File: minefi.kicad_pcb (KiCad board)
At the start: 2 copper layers, 130.8 x 95.2 mm, 152 parts, among them P1 CONN_25X2, P11 CONN_1, P13 CONN_1, P16 CONN_1, P18 CONN_1, P2 CONN_25X2, P20 CONN_1, P21 CONN_1, P23 CONN_1, P4 CONN_25, P5 CONN_3X2, P51 CONN_1, P52 CONN_1, Q1001 MOS_PRO, Q401 OVP_DRIVER, Q402 OVP_DRIVER, Q403 OVP_DRIVER, Q404 OVP_DRIVER, U1001 LM2596, U101 MAX9926/9927, U201 MCP6004, U202 MCP6004

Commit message: progress
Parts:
- removed P20, P21, P23: CONN_1, SIL-1
- C1001, C1002, C1003, D1001, D1002, D1003, D1004, D1005, D1006, L1001, L1002, Q1001, R1001, R1002, R320, R321, U1001, W23: moved to F.Cu
- moved C23 85.6 mm to (14.0, 85.1)
- moved C24 85.6 mm to (14.0, 82.5)
- moved D1002 72.2 mm to (86.4, 31.8), turned to 180 degrees
- moved D1005 71.7 mm to (102.9, 24.1), turned to 270 degrees
- moved D1003 69.0 mm to (86.4, 29.2), turned to 180 degrees
- moved R1002 67.6 mm to (102.9, 20.3), turned to 270 degrees
- moved Q1001 56.7 mm to (62.2, 11.4), turned to 0 degrees
- moved D1001 54.3 mm to (58.4, 17.8), turned to 0 degrees
- moved F1001 53.0 mm to (55.9, 5.08), turned to 0 degrees
- moved R1001 52.9 mm to (57.1, 10.2)
- moved C1001 52.1 mm to (71.1, 15.2)
- moved L1001 50.6 mm to (102.9, 8.89)
- moved R210 47.7 mm to (67.3, 59.7)
- moved R213 47.7 mm to (81.3, 58.4)
- moved R214 47.7 mm to (102.9, 58.4)
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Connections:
- P2 pad 29: /inj_12ch/INJ-10_5V -> (no net)
- P2 pad 31: /inj_12ch/INJ-07_5V -> (no net)
- P4 pad 7: /cps_vrs_io_1/CAM+ -> /cps_vrs_io_1/CAM-
- P4 pad 8: /cps_vrs_io_1/CAM- -> /cps_vrs_io_1/CAM+
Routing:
- net /adc_amp_divider/5V: track 320.7 -> 413.6 mm, vias 8 -> 5
- net GND: track 783.7 -> 849.4 mm, vias 2 -> 1
- net /stm32f407_board/3.3V: track 152.8 -> 89.8 mm
- net /adc_amp_divider/OUT4: track 14.8 -> 64.6 mm
- net /adc_amp_divider/OUT2: track 22.1 -> 60.6 mm
- net /adc_amp_divider/INP5: track 108.5 -> 71.2 mm, vias 0 -> 1
- net /adc_amp_divider/INP4: track 34.5 -> 70.5 mm
- net /adc_amp_divider/INP1: track 47.1 -> 79.9 mm, vias 1 -> 0
- net /adc_amp_divider/INP2: track 45.6 -> 74.9 mm, vias 1 -> 0
- net /adc_amp_divider/OUT3: track 25.8 -> 54.1 mm
- net /adc_amp_divider/INP3: track 36.0 -> 63.5 mm
- net /stm32f407_board/PC11: track 140.8 -> 117.0 mm, vias 0 -> 1
- net /adc_amp_divider/INP12: track 153.9 -> 131.0 mm, vias 2 -> 0
- net /PWR_buck_12V_switcher/FB: track 62.5 -> 42.8 mm
- net N-00000181: track 21.4 -> 1.91 mm
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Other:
- net class power removed

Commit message: vias and fill zones
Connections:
- hole1 pad 1: (no net) -> GND
- hole2 pad 1: (no net) -> GND
- hole3 pad 1: (no net) -> GND
- hole4 pad 1: (no net) -> GND
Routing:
- net GND: track 849.4 -> 865.8 mm
- net /PWR_buck_12V_switcher/VBAT: track 42.6 -> 38.8 mm
- net /PWR_buck_12V_switcher/Vf: track 8.54 -> 7.35 mm
- net (no net): vias 0 -> 196
- added copper zone on F.Cu, net (none)
- added copper zone on B.Cu, net GND
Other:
- net class Default: clearance 0.254 -> 0.1778
- rule trace_clearance: 0.254 -> 0.1778

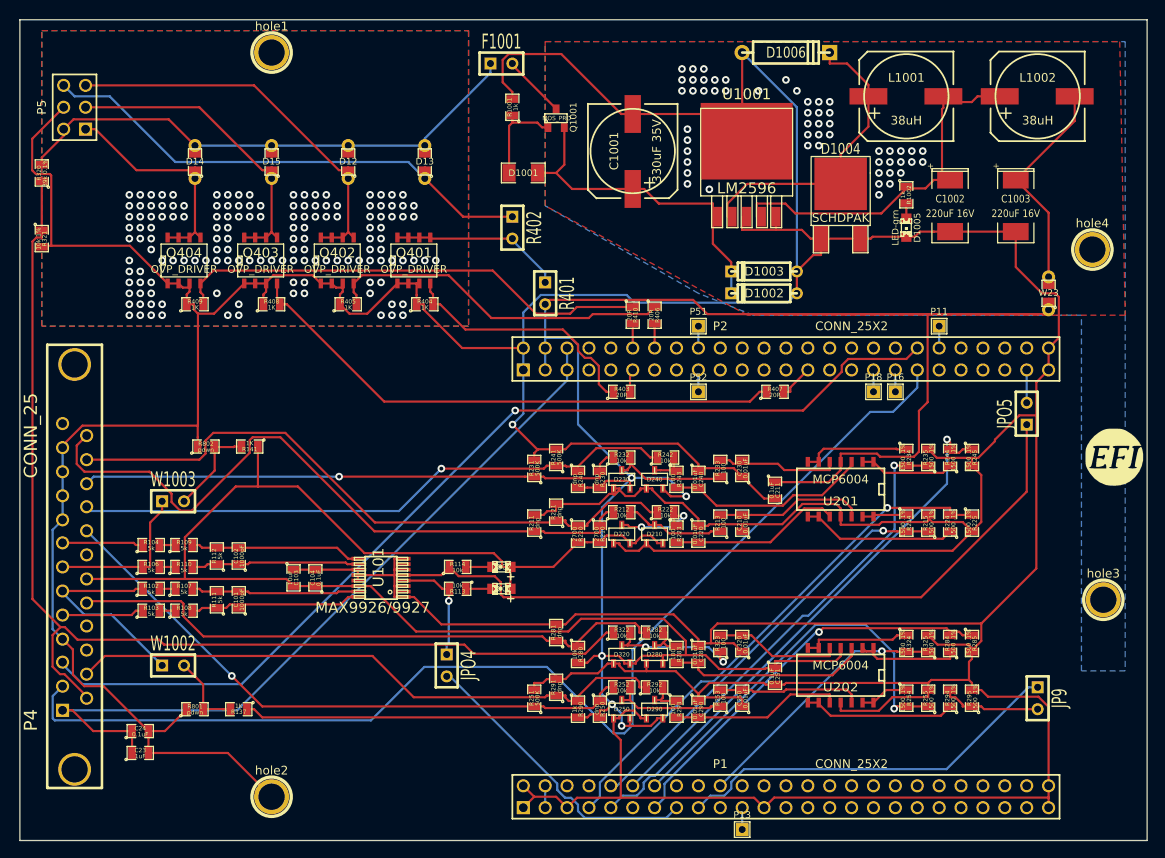
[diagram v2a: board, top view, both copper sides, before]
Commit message: more width of power lines
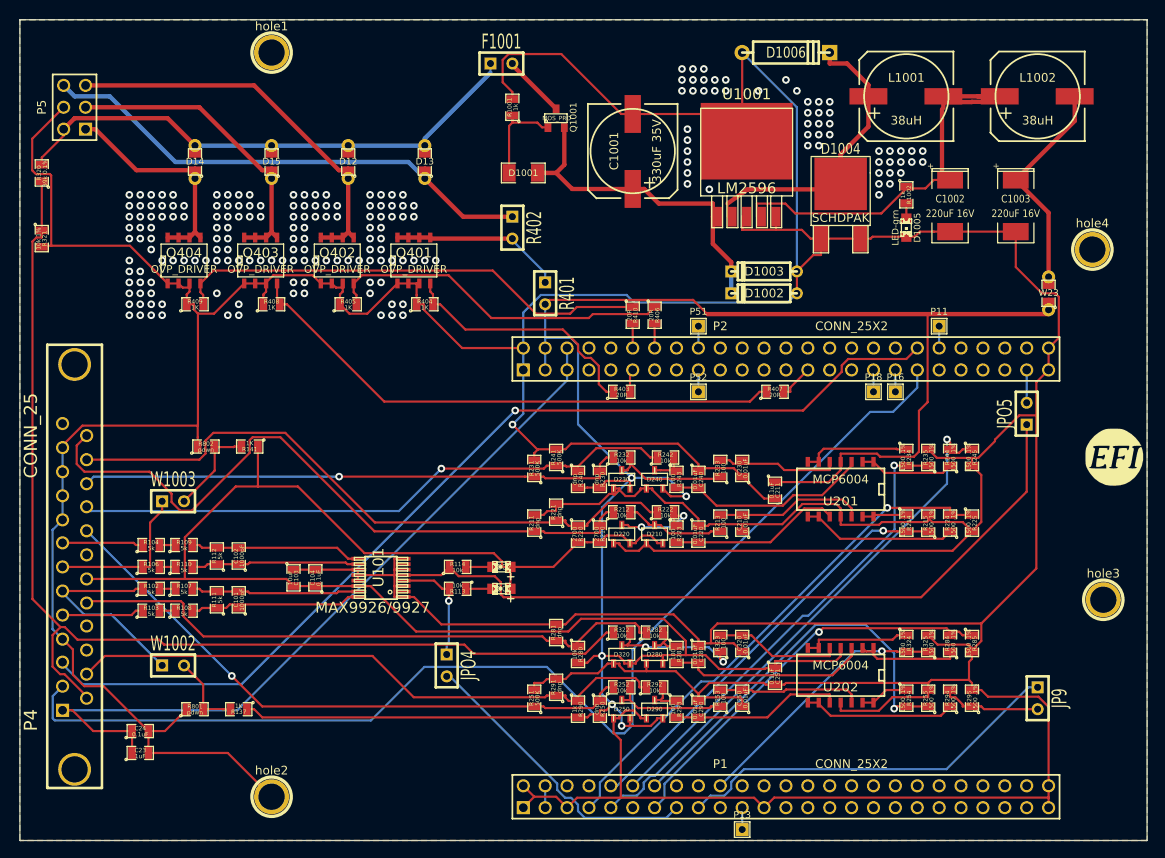
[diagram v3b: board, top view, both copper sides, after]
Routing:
- net /PWR_buck_12V_switcher/FB: track 42.8 -> 51.9 mm
- added copper zone on F.Cu, net GND
- removed copper zone on F.Cu, net (none)
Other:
- net class power added: clearance 0.1778, trace_width 0.508, via_dia 0.889, via_drill 0.635

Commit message: wider wires
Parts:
- moved P5 180.7 mm to (183.5, 45.7), turned to 0 degrees
- moved R320 175.0 mm to (175.9, 41.9), turned to 0 degrees
- moved hole1 173.2 mm to (189.9, 68.6), turned to 270 degrees
- moved R321 166.6 mm to (168.3, 41.9), turned to 180 degrees
- moved L1002 162.9 mm to (184.8, 157.5), turned to 270 degrees
- moved D14 162.7 mm to (177.2, 59.7), turned to 0 degrees
- moved F1001 160.4 mm to (188.6, 95.2), turned to 270 degrees
- moved D1006 160.3 mm to (189.9, 128.3), turned to 270 degrees
- moved D15 156.9 mm to (177.2, 68.6), turned to 0 degrees
- moved L1001 156.5 mm to (184.8, 142.2), turned to 270 degrees
- moved R1001 153.1 mm to (183.5, 96.5), turned to 0 degrees
- moved D12 151.8 mm to (177.2, 77.5), turned to 0 degrees
- moved Q1001 150.1 mm to (182.2, 101.6), turned to 270 degrees
- moved Q404 149.8 mm to (165.7, 58.4), turned to 270 degrees
- moved D13 147.7 mm to (177.2, 86.4), turned to 0 degrees
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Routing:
- net /PWR_buck_12V_switcher/FB: track 51.9 -> 49.4 mm
- net /adc_amp_divider/12V_bat: track 65.4 -> 67.6 mm
- net /inj_12ch/INJ-01_2: track 59.3 -> 57.2 mm
- net /inj_12ch/INJ-02: track 46.1 -> 47.5 mm
- net /adc_amp_divider/5V: track 413.6 -> 414.7 mm
- net /inj_12ch/INJ-01: track 20.0 -> 19.5 mm
- net (no net): vias 196 -> 190
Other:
- board size 130.8 x 95.2 mm -> 95.3 x 130.8 mm
- net class power: trace_width 0.508 -> 0.762

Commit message: progress
board is better
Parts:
- moved D14 57.2 mm to (135.1, 98.6)
- moved D12 53.6 mm to (135.1, 110.7)
- moved D15 48.1 mm to (142.2, 101.6), turned to 180 degrees
- moved D210 46.4 mm to (102.0, 146.6)
- moved D220 46.4 mm to (102.0, 142.8)
- moved D230 46.4 mm to (108.3, 142.8)
- moved D240 46.4 mm to (108.3, 146.6)
- moved D802 46.4 mm to (98.2, 128.8)
- moved R223 46.4 mm to (102.0, 149.1)
- moved R243 46.4 mm to (108.3, 149.1)
- moved R802 46.4 mm to (112.1, 94.5)
- moved C1002 46.4 mm to (140.1, 180.9)
- moved C1003 46.4 mm to (140.1, 188.5)
- moved C210 46.4 mm to (103.3, 156.7)
- moved C211 46.4 mm to (107.1, 160.6)
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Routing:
- net GND: track 865.8 -> 1084.0 mm, vias 1 -> 99
- net /inj_12ch/INJ-03_5V: track 4.21 -> 72.2 mm
- net /inj_12ch/INJ-04_5V: track 2.86 -> 59.4 mm, vias 0 -> 1
- net N-00000131: track 64.4 -> 12.5 mm
- net N-00000129: track 55.7 -> 4.78 mm
- net /inj_12ch/INJ-02_5V: track 2.86 -> 48.6 mm
- net /inj_12ch/INJ-01_5V: track 2.67 -> 38.9 mm
- net N-00000127: track 40.5 -> 4.78 mm
- net /adc_amp_divider/5V: track 414.7 -> 432.3 mm
- net N-00000132: track 29.4 -> 12.6 mm
- net /adc_amp_divider/12V_bat: track 67.6 -> 79.9 mm
- net /inj_12ch/INJ-01_2: track 57.2 -> 46.4 mm
- net /inj_12ch/INJ-01: track 19.5 -> 12.8 mm
- net /inj_12ch/INJ-04: track 26.6 -> 33.1 mm
- net /inj_12ch/INJ-03: track 36.5 -> 30.7 mm
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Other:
- net class .02 added: clearance 0.2032, trace_width 0.508, via_dia 0.889, via_drill 0.635
- net class Default: clearance 0.1778 -> 0.2032
- net class power removed
- rule pad_to_mask_clearance: 0.2 -> 0
- rule trace_clearance: 0.1778 -> 0.2032

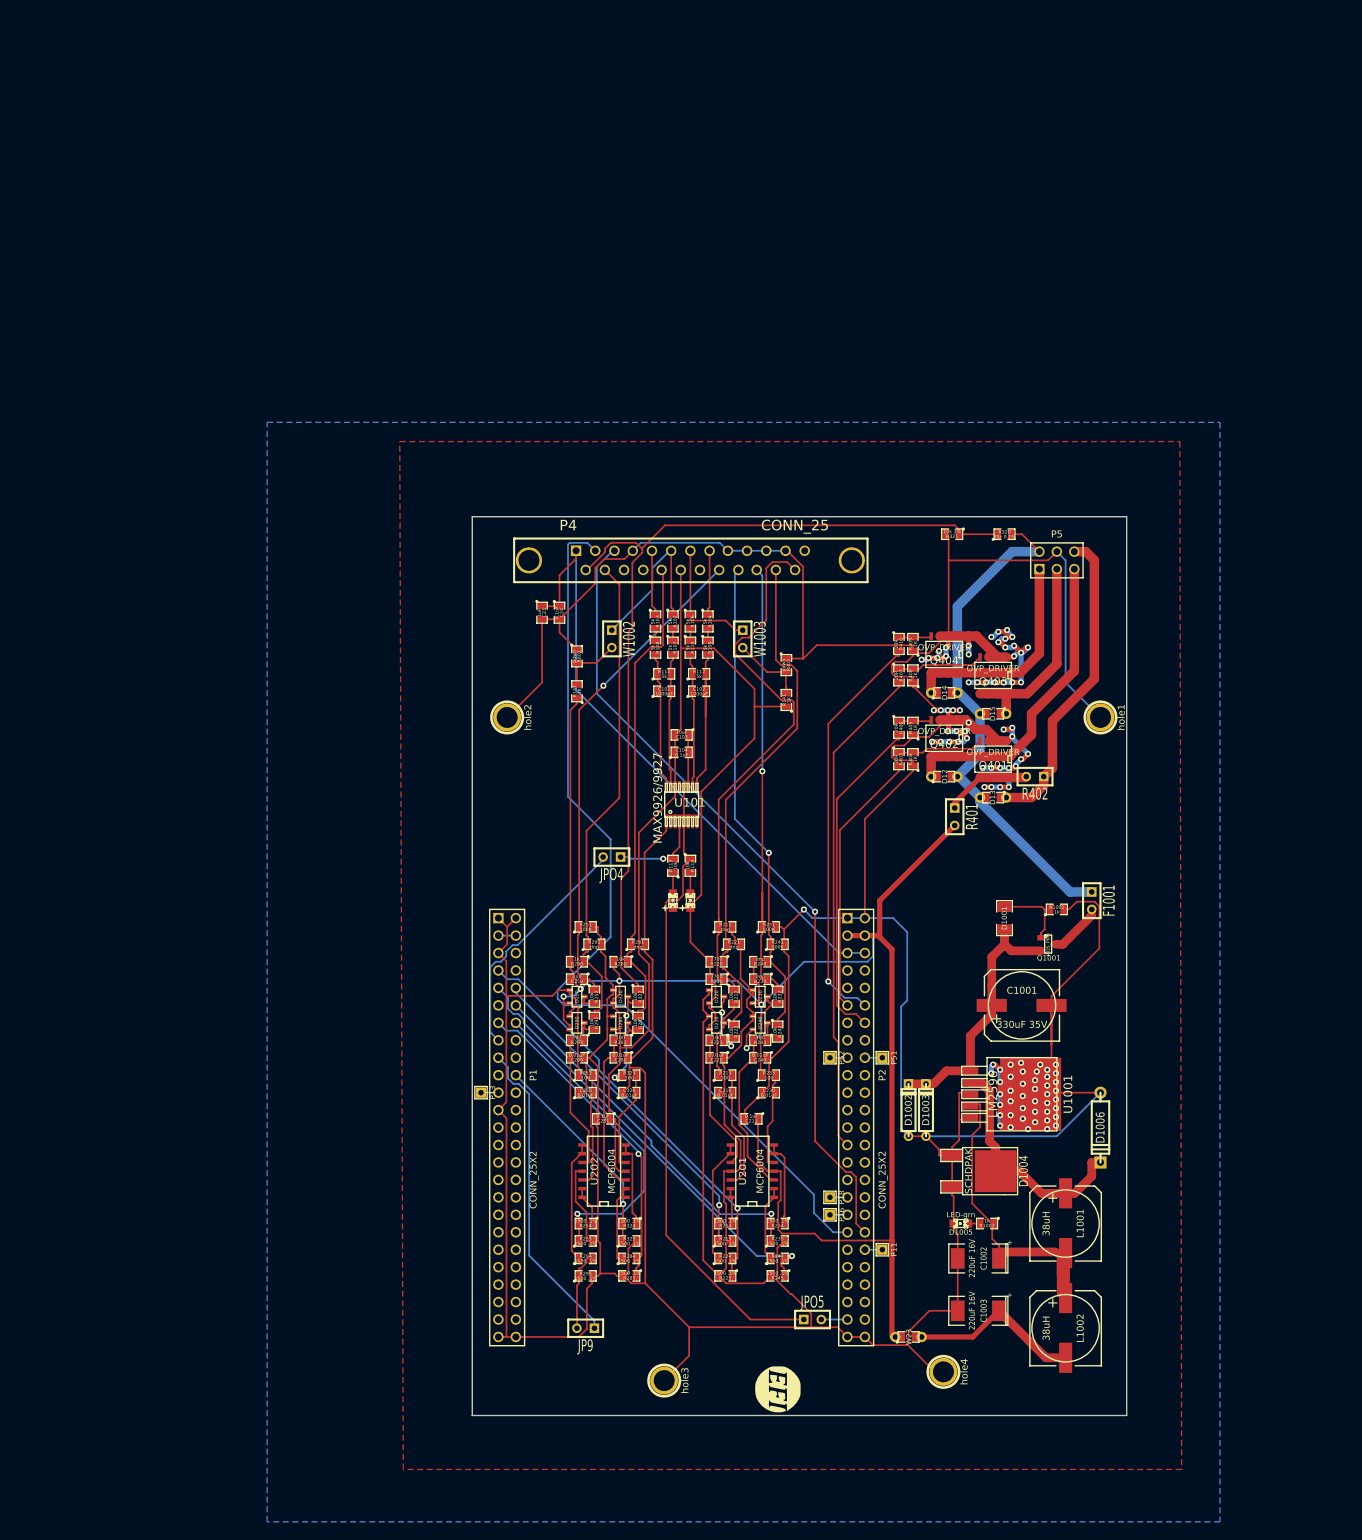
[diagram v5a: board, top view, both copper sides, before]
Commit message: vr input changed to lm1815
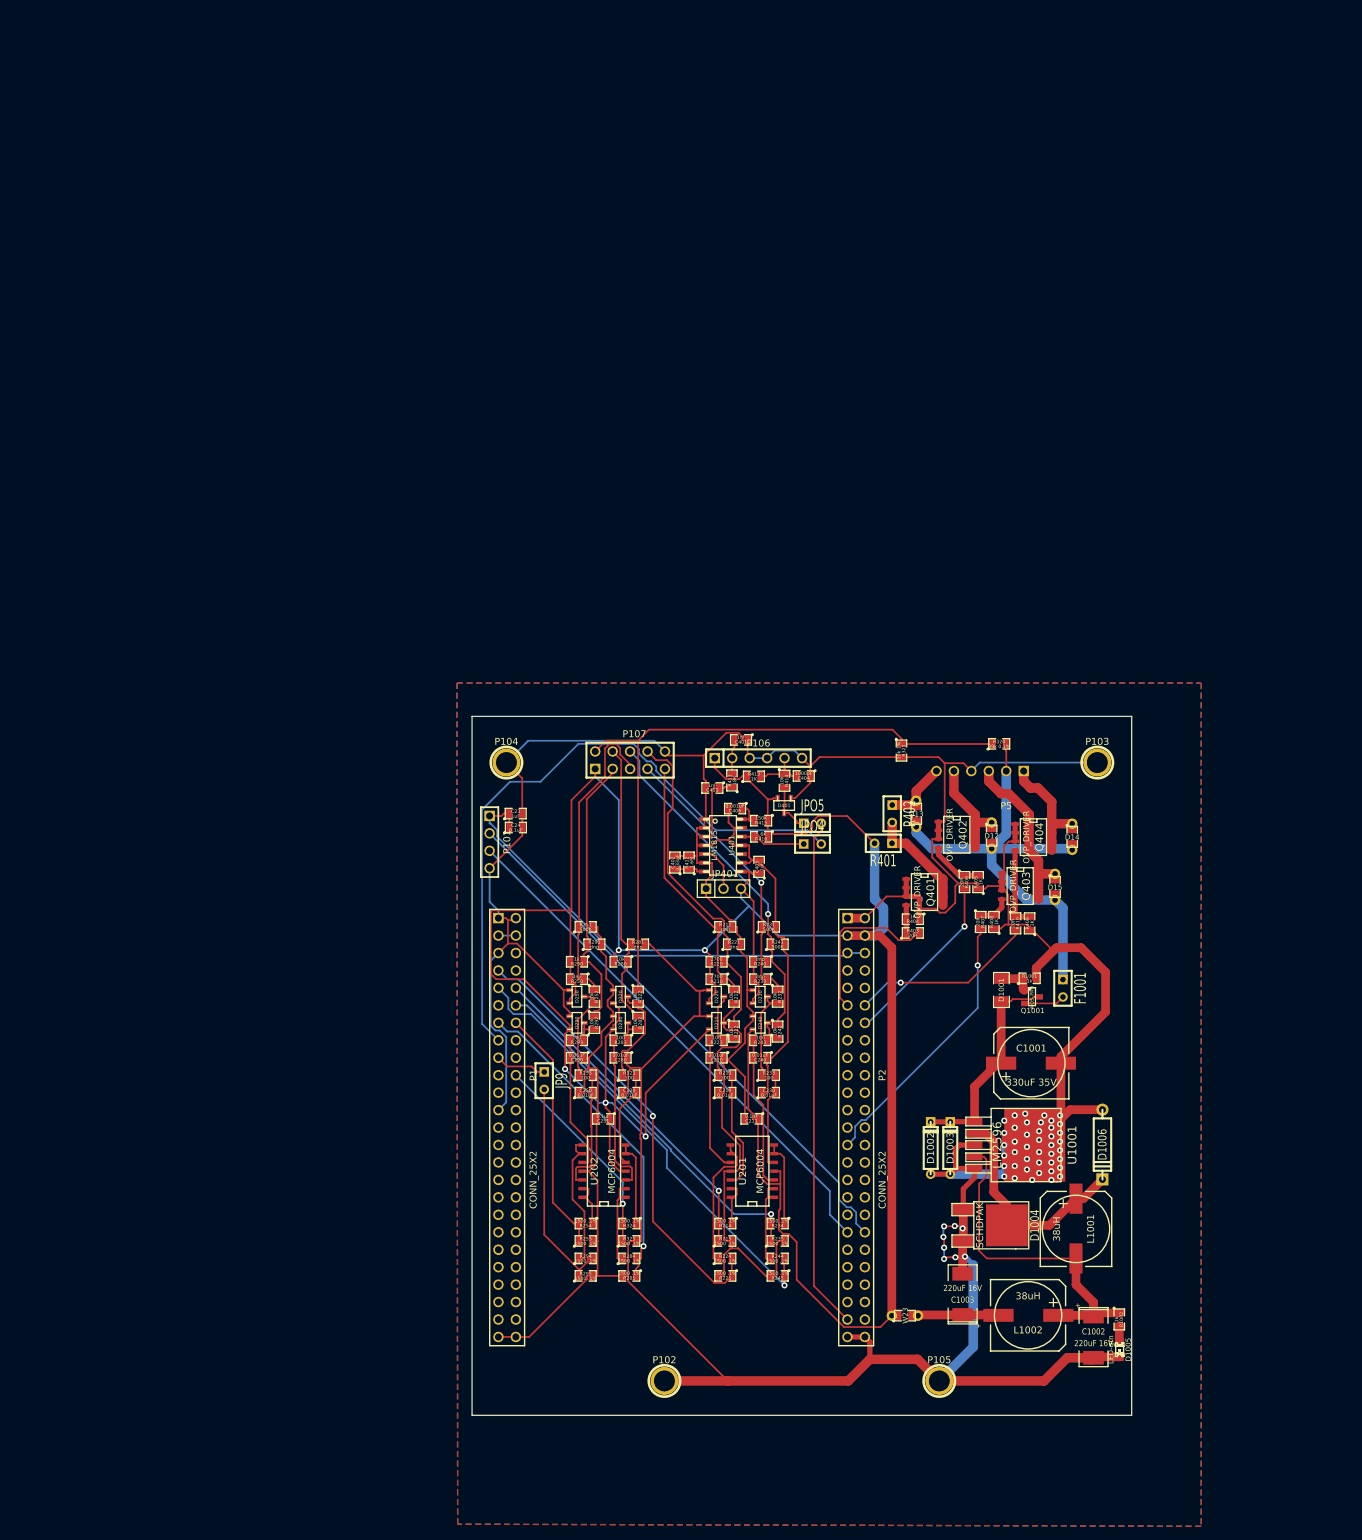
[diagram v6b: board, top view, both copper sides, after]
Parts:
- removed C101, C102: 1000pF, SM0805
- removed C103: 10uF, SM0805
- removed C104: 0.1uF, SM0805
- removed D801, D802: LED-red, LED-0805_A
- removed G1: LOGO, LOGO_F
- removed G2: LOGO, LOGO
- removed P11, P13, P16, P18, P51, P52: CONN_1, SIL-1
- removed P4: CONN_25, DB25MD
- removed R102, R103, R104, R106, R107, R108, R109, R110, R111, R112: 5k, SM0805
- removed R113, R114: 10k, SM0805
- removed R137, R141: 1K, SM0805
- removed R801, R802: pdwn, SM0805
- removed U101: MAX9926/9927, maxim-10-QSOP16
- removed W1002, W1003: JMP, SIL-2
- removed hole1: H1, 1pin
- removed hole2: H2, 1pin
- removed hole3: H3, 1pin
- removed hole4: H4, 1pin
- added C401: 1nF, SM0805, F.Cu at (105.5, 105.4)
- added C402: 0.33uF, SM0805, F.Cu at (95.9, 123.2)
- added C403: 1nF, SM0805, F.Cu at (101.4, 112.4)
- added C404: 1000pF, SM0805, F.Cu at (114.7, 110.7)
- added C405: 1uF, SM0805, F.Cu at (108.2, 123.9)
- added C406: 0.001uF, SM0805, F.Cu at (104.7, 115.4)
- added D401: DOUBLE_SCHOTTKY, sot23, F.Cu at (111.8, 115.0)
- added JP401: JP_3Way, PIN_ARRAY_3X1, F.Cu at (103.0, 127.0)
- added P101: CONN_4, PIN_ARRAY_4x1, F.Cu at (69.0, 120.3)
- added P102: CONN_1, 1pin, F.Cu at (94.4, 198.7)
- added P103: CONN_1, 1pin, F.Cu at (157.4, 108.7)
- added P104: CONN_1, 1pin, F.Cu at (71.4, 108.7)
- added P105: CONN_1, 1pin, F.Cu at (134.4, 198.7)
- added P106: CONN_6, PIN_ARRAY-6X1, F.Cu at (108.1, 108.0)
- added P107: CONN_10, PIN_ARRAY_5x2_M, F.Cu at (89.4, 108.3)
- added R411: 18K, SM0805, F.Cu at (104.2, 111.3)
- added R412: 1.6M, SM0805, F.Cu at (98.0, 123.2)
- added R413: 1K, SM0805, F.Cu at (107.4, 110.7)
- added R414: 10k, SM0805, F.Cu at (111.9, 111.3)
- added R415: 150K, SM0805, F.Cu at (108.5, 117.2)
- added R416: 5.6K, SM0805, F.Cu at (108.5, 119.5)
- added U401: LM1815, AB2_SO14, F.Cu at (102.9, 120.8)
- moved JPO5 72.2 mm to (116.0, 117.5)
- moved R409 44.1 mm to (147.6, 132.1)
- moved R410 44.1 mm to (145.5, 132.1)
- moved R407 37.8 mm to (140.4, 131.9)
- moved R408 37.8 mm to (142.3, 131.9)
- moved JP9 36.5 mm to (76.9, 155.0), turned to 270 degrees
- moved P5 32.8 mm to (144.2, 111.2), turned to 180 degrees
- moved R321 32.3 mm to (128.9, 107.0), turned to 270 degrees
- moved C24 31.9 mm to (72.8, 118.2), turned to 0 degrees
- moved Q403 30.9 mm to (146.2, 126.7), turned to 270 degrees
- moved R320 30.5 mm to (143.1, 106.0)
- moved Q404 29.6 mm to (148.1, 119.5), turned to 270 degrees
- moved D1005 29.5 mm to (160.7, 194.2), turned to 270 degrees
- moved C23 29.5 mm to (72.8, 116.1), turned to 0 degrees
- moved JPO4 29.3 mm to (116.0, 120.5), turned to 0 degrees
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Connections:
- net /stm32f407_board/3.3V renamed /3.3V
- net /stm32f407_board/PA5 renamed /PA5
- net /stm32f407_board/PC6 renamed /PC6
- net /stm32f407_board/VDD renamed /VDD
- P1 pad 21: /stm32f407_board/PB1 -> (no net)
- P2 pad 17: /stm32f407_board/PE0 -> (no net)
- P2 pad 18: /stm32f407_board/PE1 -> (no net)
- P2 pad 33: /stm32f407_board/PD1 -> (no net)
- P2 pad 35: /stm32f407_board/PC12 -> (no net)
- P2 pad 37: /stm32f407_board/PC10 -> /PC10
- P2 pad 38: /stm32f407_board/PC11 -> /PC11
- P2 pad 40: /stm32f407_board/PA15 -> (no net)
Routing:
- net GND: track 1084.0 -> 895.0 mm, vias 99 -> 50
- net /stm32f407_board/PC10: track 134.2 -> 0.00 mm
- net /stm32f407_board/PC11: track 117.0 -> 0.00 mm, vias 1 -> 0
- net /PC11: track 0.00 -> 81.0 mm
- net /cps_vrs_io_1/CAM: track 87.8 -> 7.40 mm
- net /PC10: track 0.00 -> 77.1 mm
- net /PC6: track 3.81 -> 74.7 mm
- net /PA5: track 34.8 -> 94.6 mm
- net /adc_amp_divider/INP1: track 81.1 -> 37.6 mm
- net /adc_amp_divider/OUT9: track 45.6 -> 7.52 mm
- net /inj_12ch/INJ-01_2: track 46.4 -> 10.1 mm
- net /adc_amp_divider/INP12: track 131.6 -> 96.8 mm
- net /inj_12ch/INJ-04_5V: track 59.4 -> 26.9 mm
- net /inj_12ch/INJ-03_5V: track 72.2 -> 39.9 mm, vias 0 -> 1
- net /inj_12ch/INJ-02: track 46.5 -> 15.9 mm
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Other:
- board size 95.3 x 130.8 mm -> 96 x 101.7 mm
